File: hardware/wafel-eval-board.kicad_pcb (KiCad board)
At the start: 2 copper layers, 202.6 x 66 mm, 257 parts, among them J101 CAN PORT, J102 SW, J201 Conn_01x02, J202 Conn_01x02, J203 Conn_01x02, J204 Conn_01x02, J205 Conn_01x02, J801 UART1, Q1001 CJ3134K, Q101 AO3422, Q1101 CJ3134K, Q1201 CJ3134K, Q1301 CJ3134K, Q1401 CJ3134K, Q1501 CJ3134K, Q1601 CJ3134K, Q1701 CJ3134K, Q1801 CJ3134K, Q1901 CJ3134K, Q201 NPN, Q202 2N7002K, Q301 IRLML6402, Q302 2N7002K, Q401 IPB085N15NM6, Q402 IPB085N15NM6, Q403 IPB085N15NM6, Q501 IPB085N15NM6, Q502 IPB085N15NM6, Q503 IPB085N15NM6, Q601 PJM10H01PSA, Q701 PJM10H01PSA, Q901 ZXMP10A13FTA, Q902 2N7002K, SW801 SW_Push, U101 LM5163DDA, U201 BQ7694204, U801 NUCLEO-L432KC, U802 TCAN1043A, U803 TLP241A

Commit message: no 70 warns
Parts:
- moved Q1601 0.30 mm to (97.6, 97.7)
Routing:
- net (no net): track 0.87 -> 0.00 mm
- net /Frontend/DSG: track 91.8 -> 90.9 mm
- net /CB Mosfets/CELL6: track 17.3 -> 17.9 mm
- net GND: vias 195 -> 202

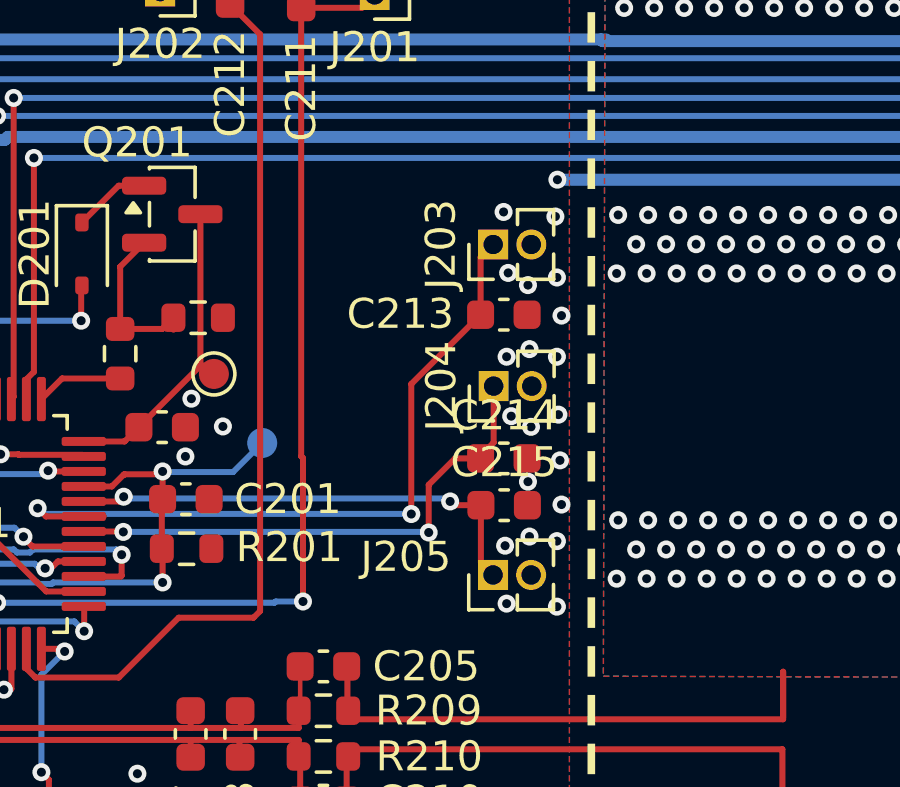
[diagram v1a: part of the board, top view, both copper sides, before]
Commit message: no 79 warns
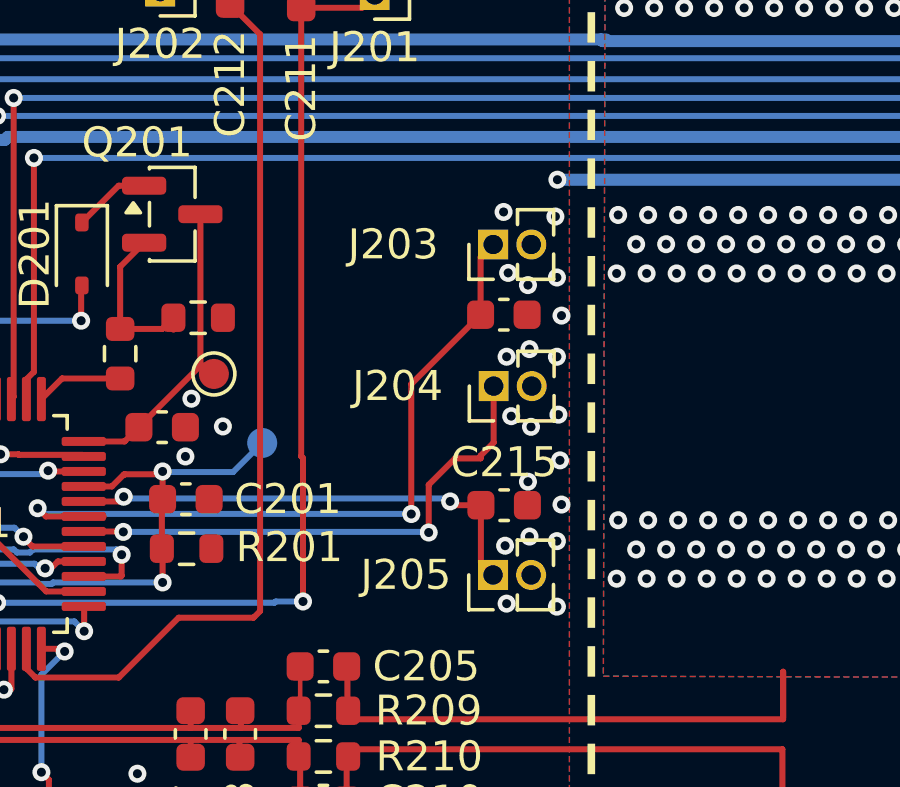
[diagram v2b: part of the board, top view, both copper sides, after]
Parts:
- removed C214: 470p, Capacitor_SMD:C_0603_1608Metric
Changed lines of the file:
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@@
 		(tags "Through hole pin header THT 1x02 1.27mm single row")
 		(property "Reference" "J203"
-			(at 0 -1.745 90)
+			(at 0 -3.335 180)
 			(layer "F.SilkS")
 			(effects
@@
 			(at -3.45 -0.025 0)
 			(layer "F.SilkS")
+			(hide yes)
 			(effects
 				(font
@@
 		(tags "Through hole pin header THT 1x02 1.27mm single row")
 		(property "Reference" "J204"
-			(at 0 -1.745 90)
+			(at 0 -3.2 180)
 			(layer "F.SilkS")
 			(effects
@@
 		)
 	)
-	(footprint "Capacitor_SMD:C_0603_1608Metric"
-		(layer "F.Cu")
-		(at 149.615 76.49)
-		(descr "Capacitor SMD 0603 (1608 Metric), square (rectangular) end terminal, IPC-7351 nominal, (Body size source: IPC-SM-782 page 76, https://www.pcb-3d.com/wordpress/wp-content/uploads/ipc-sm-782a_amendment_1_and_2.pdf)")
-		(tags "capacitor")
-		(property "Reference" "C214"
-			(at 0 -1.43 0)
-			(layer "F.SilkS")
-			(effects
-				(font
-					(size 1 1)
-					(thickness 0.15)
-				)
-			)
-		)
-		(property "Value" "470p"
-			(at 0 1.43 0)
-			(layer "F.Fab")
-			(effects
-				(font
-					(size 1 1)
-					(thickness 0.15)
-				)
-			)
-		)
-		(property "Datasheet" ""
-			(at 0 0 0)
-			(layer "F.Fab")
-			(hide yes)
-			(effects
-				(font
-					(size 1.27 1.27)
-				)
-			)
-		)
-		(property "Description" "Unpolarized capacitor, small symbol"
-			(at 0 0 0)
-			(layer "F.Fab")
-			(hide yes)
-			(effects
-				(font
-					(size 1.27 1.27)
-				)
-			)
-		)
-		(property "KiLib_Generator" "SMD_2terminal_chip_molded"
-			(at 0 0 0)
-			(layer "F.SilkS")
-			(hide yes)
-			(effects
-				(font
-					(size 1 1)
-					(thickness 0.15)
-				)
-			)
-		)
-		(property ki_fp_filters "C_*")
-		(sheetname "/Frontend/")
-		(sheetfile "frontend.kicad_sch")
-		(units
-			(unit
-				(name "A")
-				(pins "1" "2")
-			)
-		)
-		(attr smd)
-		(duplicate_pad_numbers_are_jumpers no)
-		(fp_line
-			(start -0.14058 -0.51)
-			(end 0.14058 -0.51)
-			(stroke
-				(width 0.12)
-				(type solid)
-			)
-			(layer "F.SilkS")
-		)
-		(fp_line
-			(start -0.14058 0.51)
-			(end 0.14058 0.51)
-			(stroke
-				(width 0.12)
-				(type solid)
-			)
-			(layer "F.SilkS")
-		)
-		(fp_rect
-			(start -1.48 -0.73)
-			(end 1.48 0.73)
-			(stroke
-				(width 0.05)
-				(type solid)
-			)
-			(fill no)
-			(layer "F.CrtYd")
-		)
-		(fp_rect
-			(start -0.8 -0.4)
-			(end 0.8 0.4)
-			(stroke
-				(width 0.1)
-				(type solid)
-			)
-			(fill no)
-			(layer "F.Fab")
-		)
-		(fp_text user "${REFERENCE}"
-			(at 0 0 0)
-			(layer "F.Fab")
-			(effects
-				(font
-					(size 0.4 0.4)
-					(thickness 0.06)
-				)
-			)
-		)
-		(pad "1" smd roundrect
-			(at -0.775 0)
-			(size 0.9 0.95)
-			(layers "F.Cu" "F.Mask" "F.Paste")
-			(roundrect_rratio 0.25)
-			(net "/Frontend/TS4")
-			(pintype "passive")
-		)
-		(pad "2" smd roundrect
-			(at 0.775 0)
-			(size 0.9 0.95)
-			(layers "F.Cu" "F.Mask" "F.Paste")
-			(roundrect_rratio 0.25)
-			(net "GND")
-			(pintype "passive")
-		)
-		(embedded_fonts no)
-		(model "${KICAD10_3DMODEL_DIR}/Capacitor_SMD.3dshapes/C_0603_1608Metric.stpZ"
-			(offset
-				(xyz 0 0 0)
-			)
-			(scale
-				(xyz 1 1 1)
-			)
-			(rotate
-				(xyz 0 0 0)
-			)
-		)
-	)
 	(footprint "Resistor_SMD:R_0603_1608Metric"
 		(layer "F.Cu")
@@
 		(tags "Through hole pin header THT 1x02 1.27mm single row")
 		(property "Reference" "J205"
-			(at 0.6 -2.905 180)
+			(at 0 -2.905 180)
 			(layer "F.SilkS")
 			(effects

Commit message: add thermal vias
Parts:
- moved F103 18.4 mm to (234.6, 102.8)
- moved H117 6.90 mm to (241.0, 107.7)
- moved F102 2.25 mm to (247.9, 102.9)
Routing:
- net /High-Side N-MOSFET/MOSFET-CASCADE-CHG/DRAIN: track 82.7 -> 64.4 mm, vias 79 -> 171
- net Net-(F103-Pad4): track 14.3 -> 25.3 mm
- net /xBAT+: vias 52 -> 50

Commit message: kelvin connect
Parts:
- moved R105 5.90 mm to (177.3, 85.7)
- moved R104 0.15 mm to (165.2, 85.7)
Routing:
- net /BAT-: track 17.4 -> 44.7 mm
- net PGND: track 41.6 -> 66.7 mm
